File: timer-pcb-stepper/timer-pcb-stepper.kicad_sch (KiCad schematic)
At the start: 27 parts, among them J1 JST_05, J10 JST_05, J11 JST_04, J2 battery, J3 On/off, J4 JST_03, J5 JST_03, J6 JST_03, J7 JST_03, J8 JST_03_Led_panel, J9 JST_05, U2 ULN2003, U3 ULN2003, U4 ULN2003

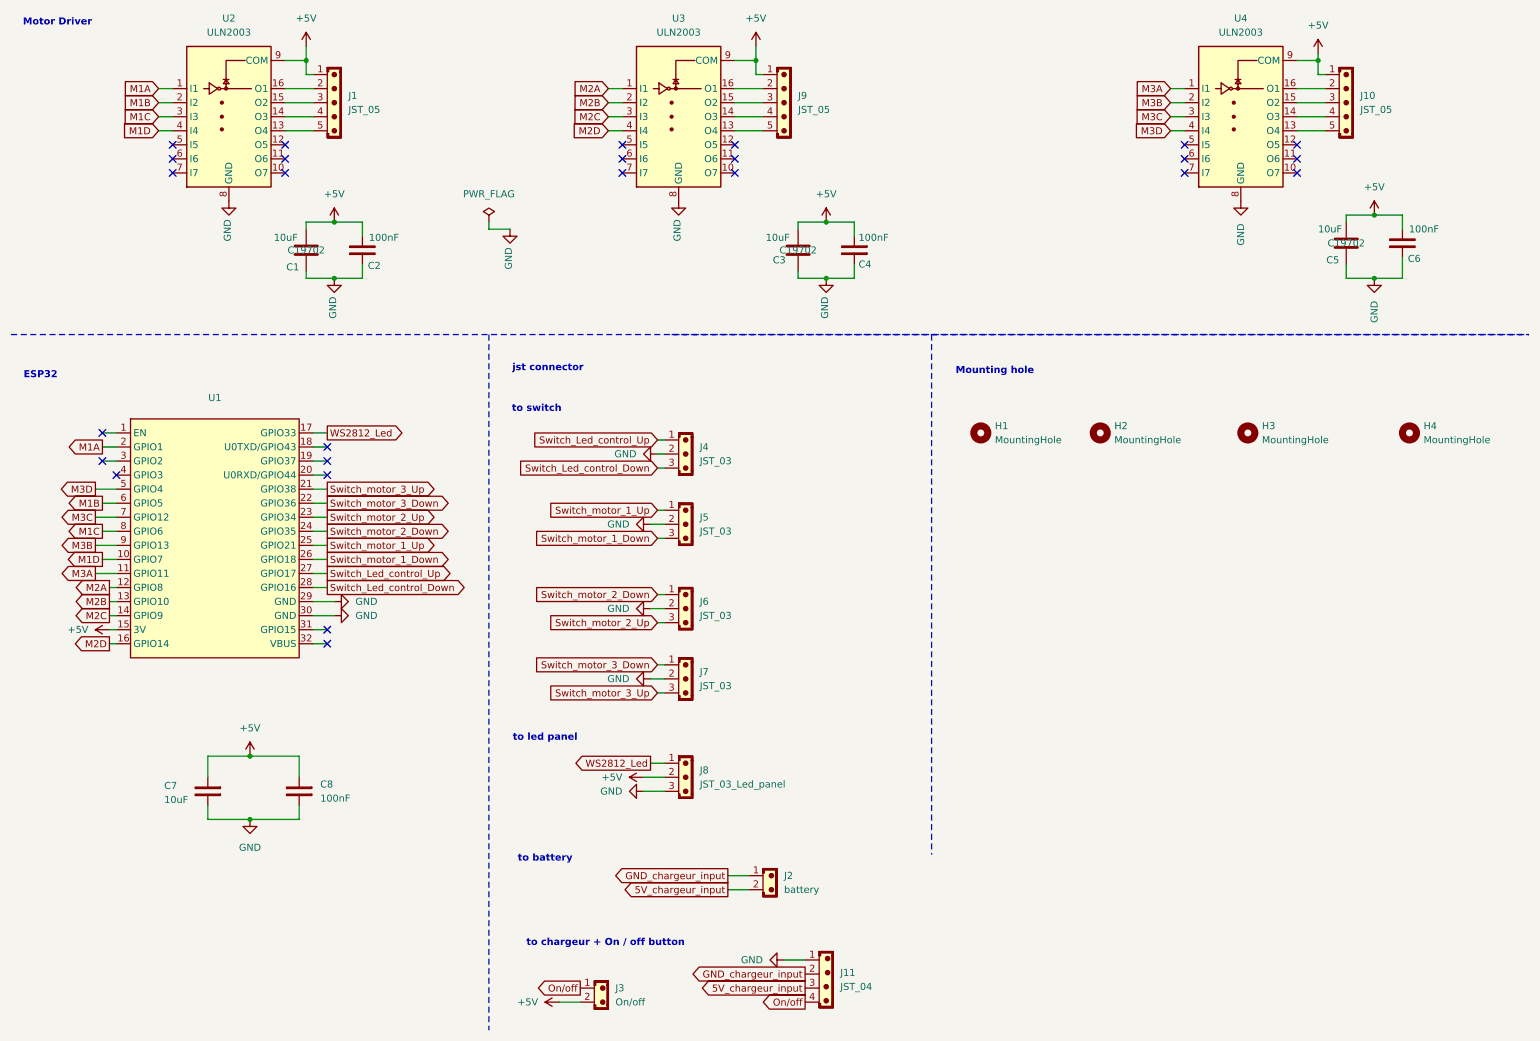
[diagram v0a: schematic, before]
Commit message: suppression du dossier chargeur. integration de la partie chargeur usb-c sur le PCB stepper
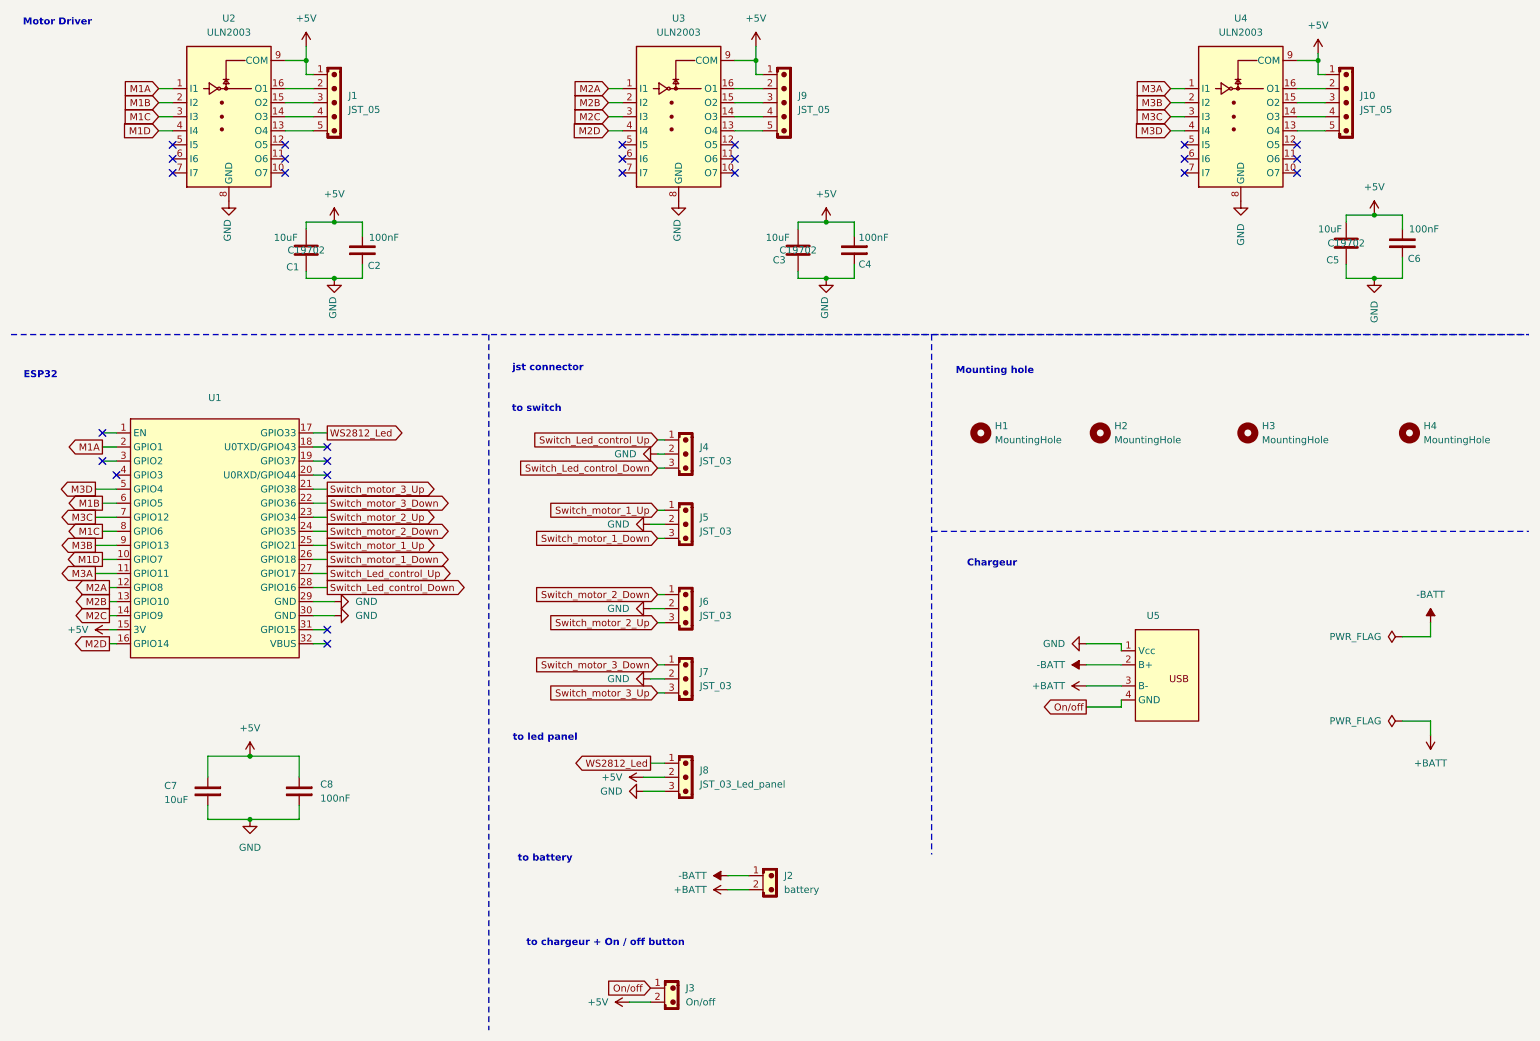
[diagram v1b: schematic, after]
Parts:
- removed J11: JST_04, Connector_JST:JST_PH_B4B-PH-K_1x04_P2.00mm_Vertical, symbol PCM_SL_Connectors:JST_04
- added U5: ~, 1_My_Custom_Library:TP4056_chargeur_USB-C, symbol 1_my_custom-_symbol_library:PCB_USB_connector
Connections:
- net GND: now also U5.1 (Vcc)
- net On/off: now also U5.4 (GND)
- net 5V_chargeur_input renamed +BATT
- net +BATT: now also U5.3 (B-)
- net GND_chargeur_input renamed -BATT
- net -BATT: now also U5.2 (B+)
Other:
- note added: "Chargeur"
- moved on the sheet: J3

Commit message: reroutage des liaisons pour avoir un circuit imprimé plus propre.
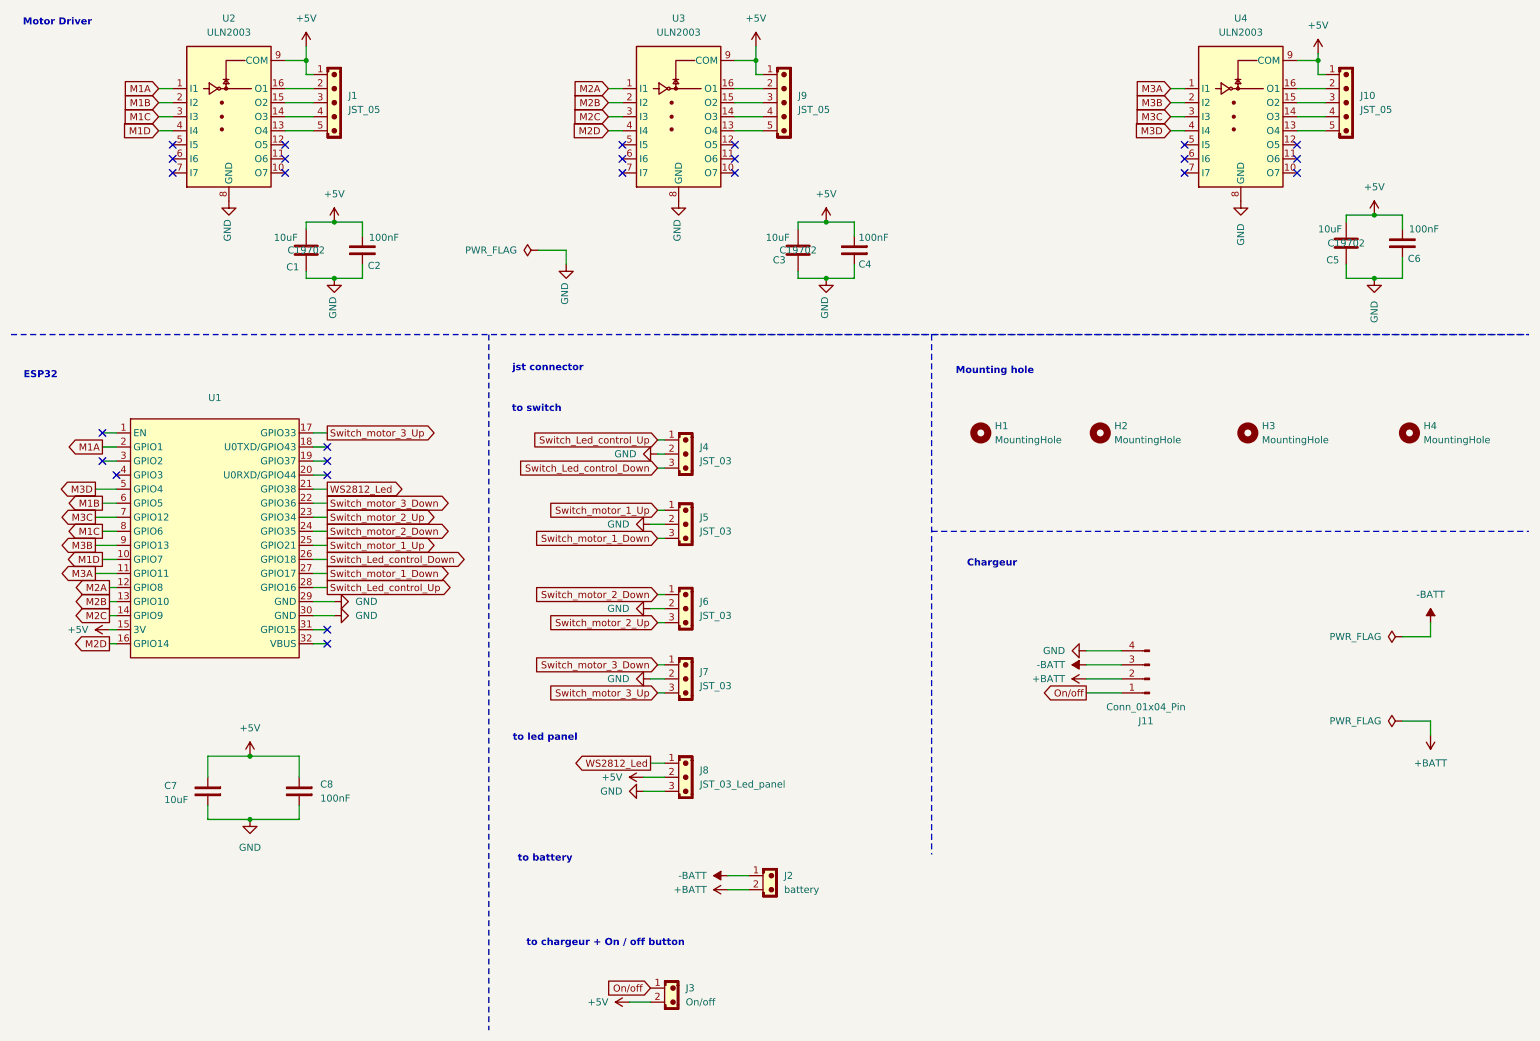
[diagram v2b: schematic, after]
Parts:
- removed U5: ~, 1_My_Custom_Library:TP4056_chargeur_USB-C, symbol 1_my_custom-_symbol_library:PCB_USB_connector
- added J11: Conn_01x04_Pin, Connector_JST:JST_XA_B04B-XASK-1-A_1x04_P2.50mm_Vertical, symbol Connector:Conn_01x04_Pin
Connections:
- net +BATT: now also J11.2 (Pin_2)
- net -BATT: now also J11.3 (Pin_3)
- net GND: now also J11.4 (Pin_4)
- net On/off: now also J11.1 (Pin_1)
- net Switch_Led_control_Down: now also U1.26 (GPIO18); no longer U1.28 (GPIO16)
- net Switch_Led_control_Up: now also U1.28 (GPIO16); no longer U1.27 (GPIO17)
- net Switch_motor_1_Down: now also U1.27 (GPIO17); no longer U1.26 (GPIO18)
- net Switch_motor_3_Up: now also U1.17 (GPIO33); no longer U1.21 (GPIO38)
- net WS2812_Led: now also U1.21 (GPIO38); no longer U1.17 (GPIO33)

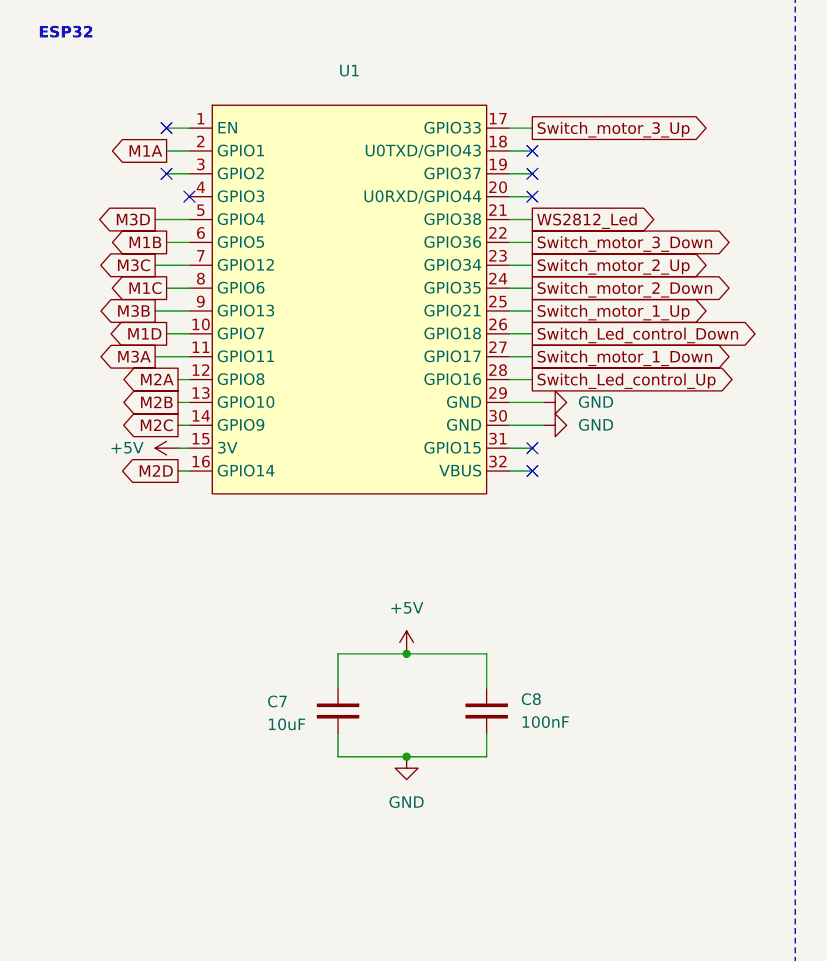
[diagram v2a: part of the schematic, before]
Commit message: ajout de text indicatif couche silkscreen sur les différents composants du PCB. ajout de test points sur 5V, GND, GPIO37 pour debugger et pin 15 (3.3V). connecteurs repositionés franc bord.
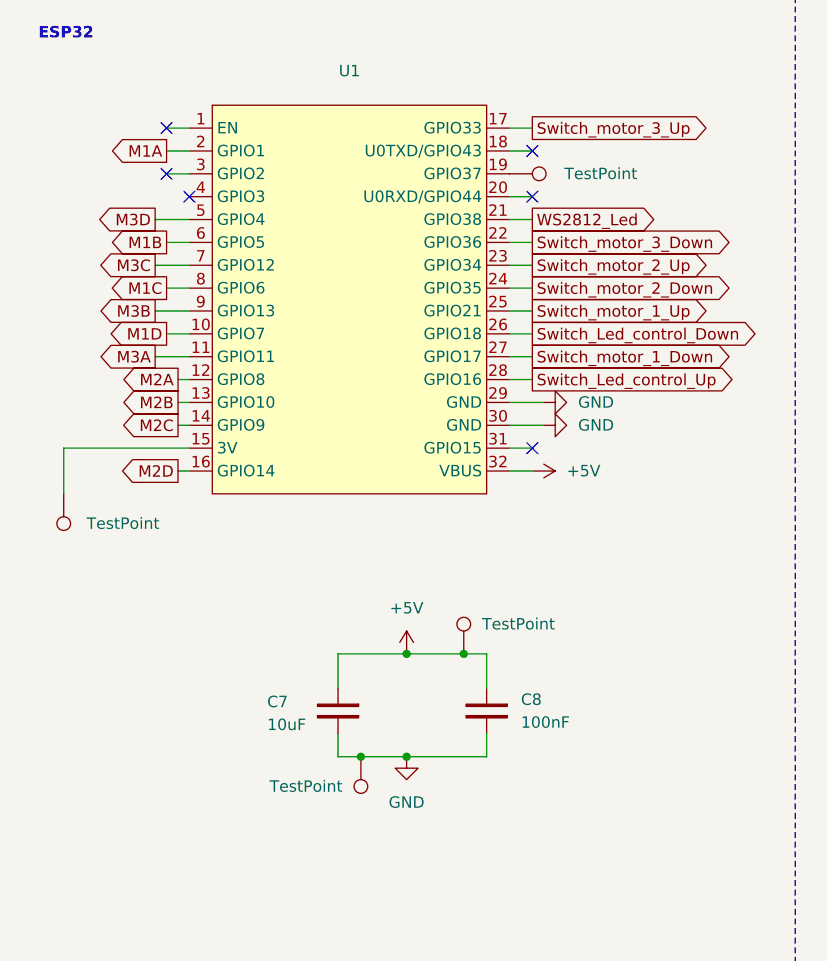
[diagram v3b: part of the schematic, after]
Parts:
- added TP1, TP2, TP3, TP4: TestPoint, TestPoint:TestPoint_Loop_D2.54mm_Drill1.5mm_Beaded, symbol Connector:TestPoint
- J2, J3: footprint Connector_JST:JST_PH_B2B-PH-K_1x02_P2.00mm_Vertical -> Connector_JST:JST_XH_B2B-XH-AM_1x02_P2.50mm_Vertical
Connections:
- net +5V: now also U1.32 (VBUS), TP2.1; no longer U1.15 (3V)
- net GND: now also TP4.1
- net at U1.19 (GPIO37): now also TP3.1
- new net: TP1.1, U1.15 (3V)
- no-connect marks 26 -> 24

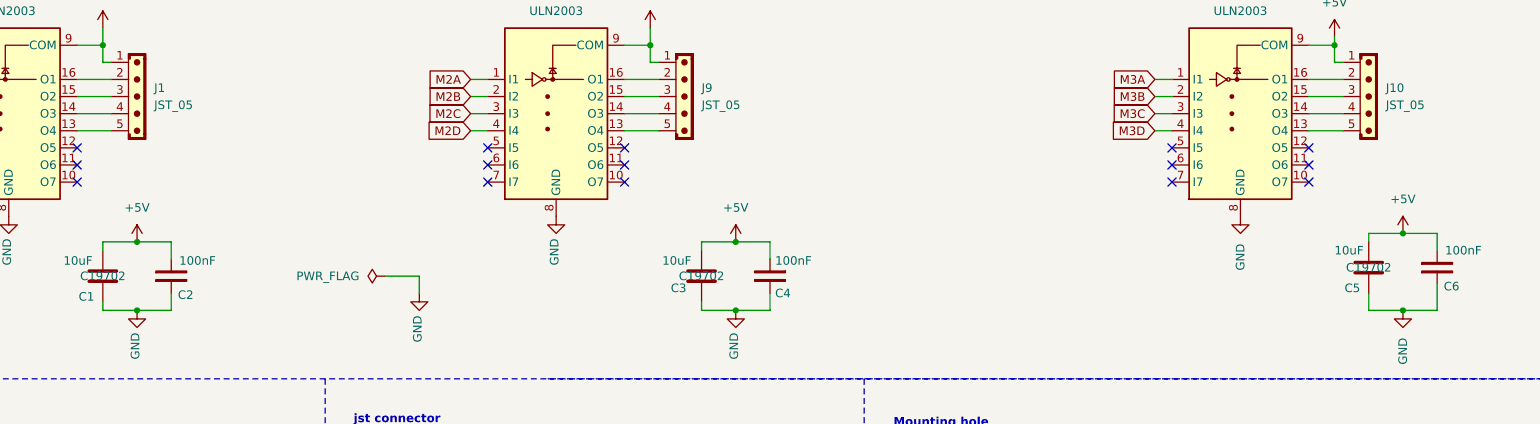
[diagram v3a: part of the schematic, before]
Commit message: ajout de text indicatif des composants, ajout de signe + et - sur la connection batterie, déplacement des connecteurs franc bord, ajout de testpoint, modification du déplacement du condensateur de découplage sur l'alimentation 5V de l'esp32
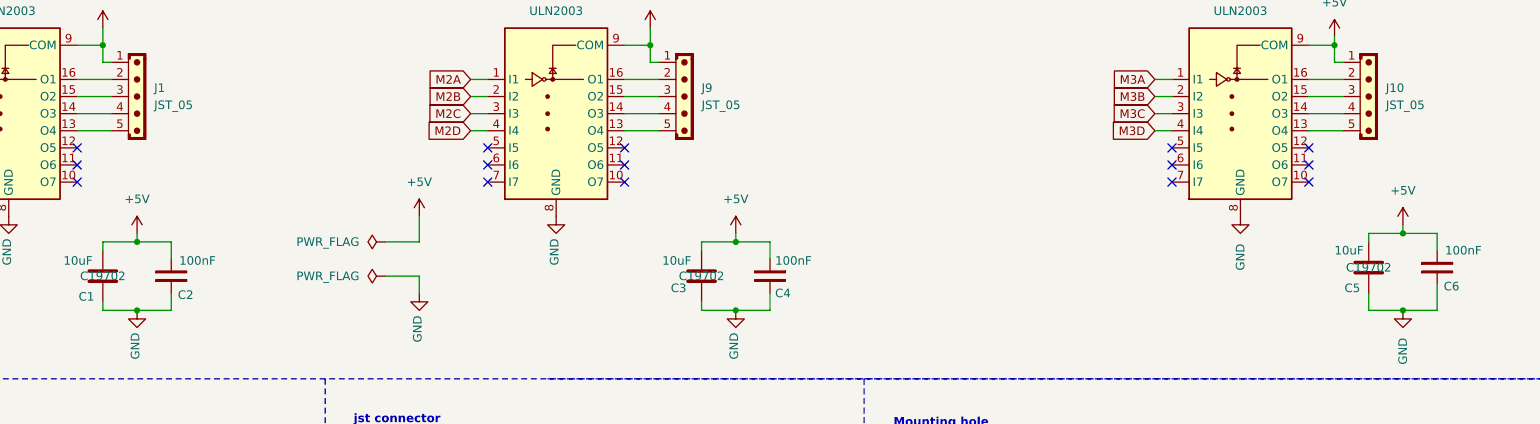
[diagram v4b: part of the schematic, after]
